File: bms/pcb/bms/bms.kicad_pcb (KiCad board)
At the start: 2 copper layers, 15 parts, among them U8 Pico

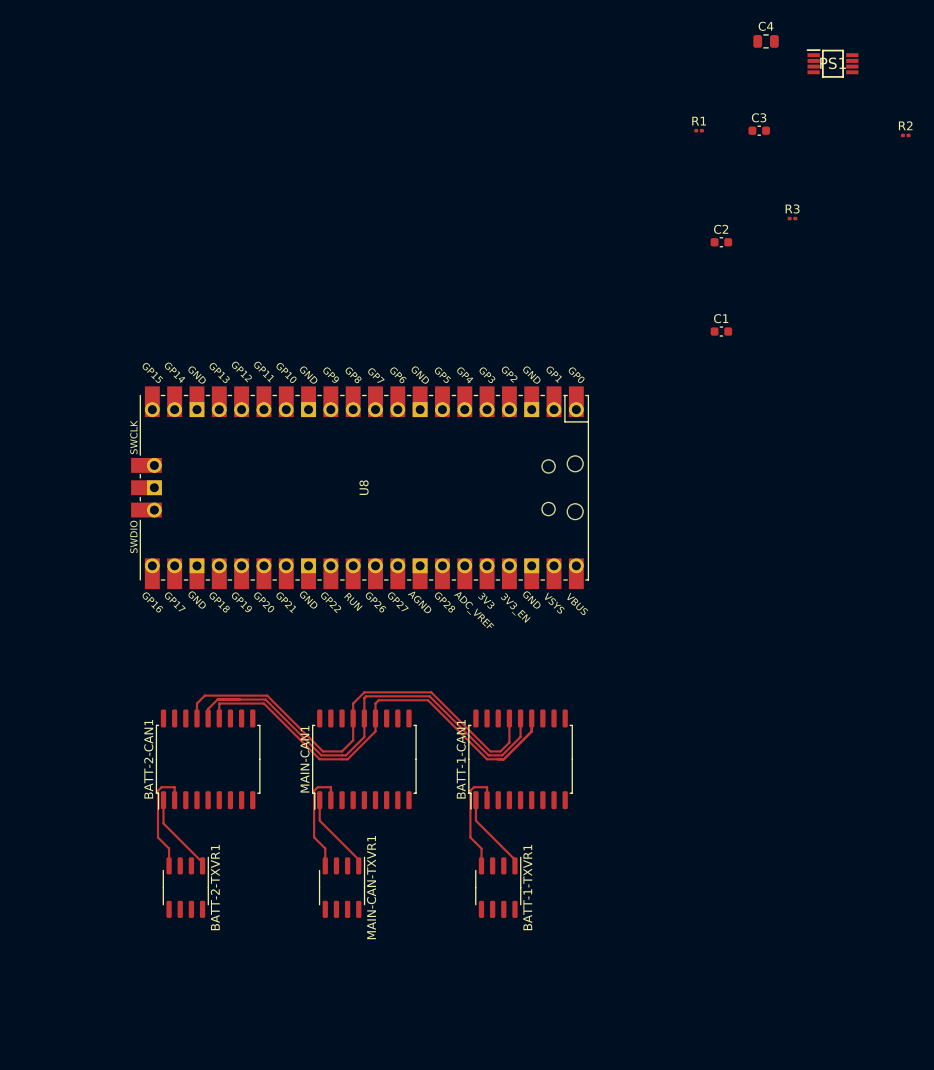
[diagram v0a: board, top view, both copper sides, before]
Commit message: v1.0 of BMS finalised. Sent of for fabrication
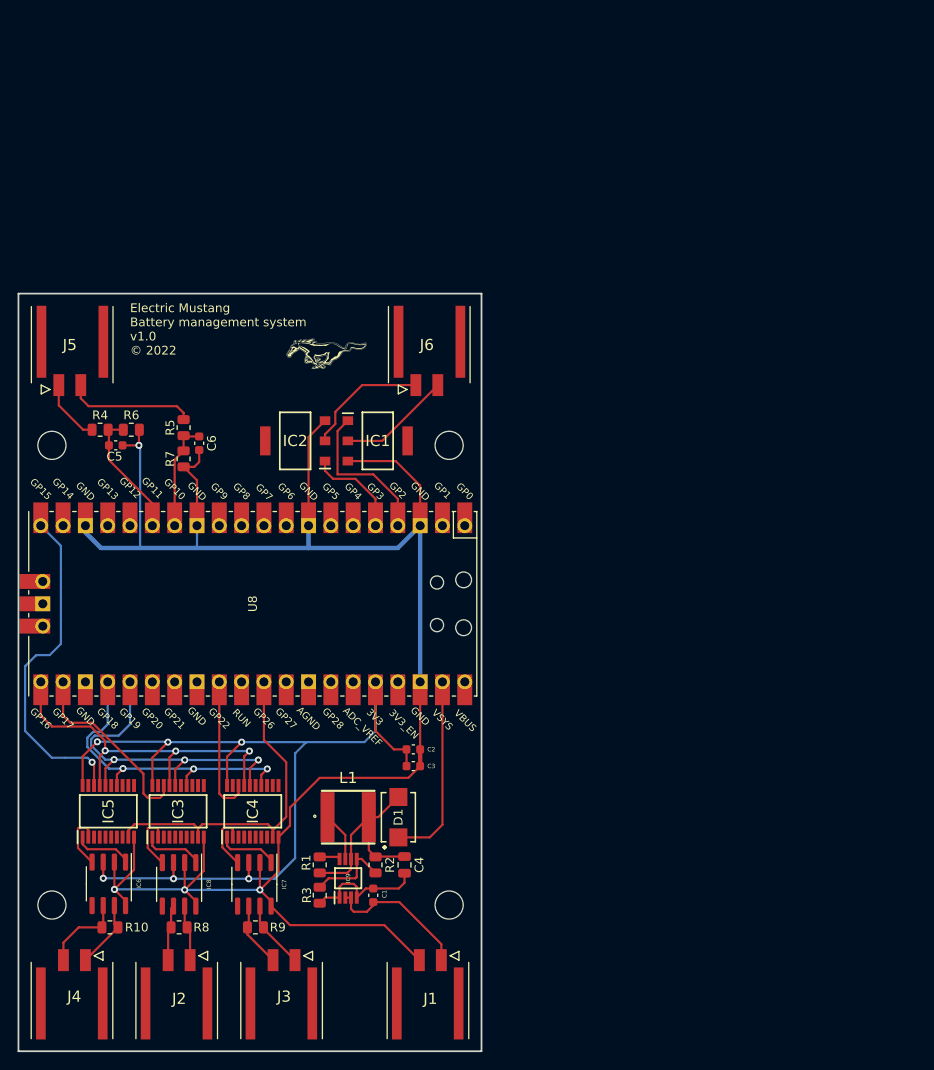
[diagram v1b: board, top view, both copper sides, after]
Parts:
- removed BATT-1-CAN1, BATT-2-CAN1, MAIN-CAN1: MCP2515-xSO, Package_SO:SOIC-18W_7.5x11.6mm_P1.27mm
- removed PS1: TPS62160DGKT, Module:SOP65P490X110-8N
- added C5: 1uF, Capacitor_SMD:C_0603_1608Metric, F.Cu at (80.9, 99.3)
- added C6: 1uF, Capacitor_SMD:C_0603_1608Metric, F.Cu at (90.4, 99.1)
- added D1: SS54B, Diode_SMD:DIOM5336X244N, F.Cu at (113.1, 141.6)
- added G***: LOGO, LOGO, F.Cu at (104.9, 88.9)
- added H1: MountingHole, MountingHole:MountingHole_3.2mm_M3, F.Cu at (73.7, 99.3)
- added H2: MountingHole, MountingHole:MountingHole_3.2mm_M3, F.Cu at (118.9, 99.3)
- added H3: MountingHole, MountingHole:MountingHole_3.2mm_M3, F.Cu at (118.9, 151.6)
- added H4: MountingHole, MountingHole:MountingHole_3.2mm_M3, F.Cu at (73.7, 151.6)
- added IC1: NCV8402ASTT1G, Symbol:SOT230P700X175-4N, F.Cu at (110.7, 98.8)
- added IC2: NCV8402ASTT1G, Symbol:SOT230P700X175-4N, F.Cu at (101.3, 98.8)
- added IC3: MCP2515-I_ST, Module:SOP65P640X120-20N, F.Cu at (88.0, 141.0)
- added IC4: MCP2515-I_ST, Module:SOP65P640X120-20N, F.Cu at (96.5, 141.0)
- added IC5: MCP2515-I_ST, Module:SOP65P640X120-20N, F.Cu at (80.1, 141.0)
- added IC9: TPS62160DGKR, Module:SOP65P490X110-8N, F.Cu at (107.4, 148.6)
- added J1: power, Connector:105430YY02, F.Cu at (116.7, 157.9)
- added J2: MAIN CAN, Connector:105430YY02, F.Cu at (88.1, 157.9)
- added J3: BATT1 CAN, Connector:105430YY02, F.Cu at (100.1, 157.9)
- added J4: BATT2 CAN, Connector:105430YY02, F.Cu at (76.2, 157.9)
- added J5: INPUTS, Connector:105430YY02, F.Cu at (75.7, 92.5)
- added J6: INPUTS, Connector:105430YY02, F.Cu at (116.3, 92.5)
- added L1: 2.2uH, Inductor_SMD:NR6028T220M, F.Cu at (107.4, 141.6)
- added R10: 120, Resistor_SMD:R_0805_2012Metric, F.Cu at (80.3, 154.2)
- added R4: 4k7, Resistor_SMD:R_0805_2012Metric, F.Cu at (79.1, 97.5)
- added R5: 4k7, Resistor_SMD:R_0805_2012Metric, F.Cu at (88.6, 97.3)
- added R6: 1k5, Resistor_SMD:R_0805_2012Metric, F.Cu at (82.7, 97.5)
- added R7: 1k5, Resistor_SMD:R_0805_2012Metric, F.Cu at (88.6, 100.9)
- added R8: 120, Resistor_SMD:R_0805_2012Metric, F.Cu at (88.1, 154.2)
- added R9: 120, Resistor_SMD:R_0805_2012Metric, F.Cu at (96.8, 154.2)
- R1, R2, R3: footprint Resistor_SMD:R_0201_0603Metric -> Resistor_SMD:R_0805_2012Metric
- moved R2 102.6 mm to (110.5, 147.1), turned to -90 degrees
- moved C4 102.4 mm to (113.8, 147.1), turned to -90 degrees
- moved R1 94.1 mm to (104.1, 147.1), turned to 90 degrees
- moved R3 94.0 mm to (104.1, 150.5), turned to -90 degrees
- moved C3 82.3 mm to (114.8, 135.8)
- moved C1 75.4 mm to (110.2, 150.5), turned to 90 degrees
- moved C2 67.5 mm to (114.8, 133.9)
- moved IC7 27.8 mm to (96.7, 149.3)
- moved IC8 18.5 mm to (88.1, 149.3)
- moved U8 18.3 mm to (96.5, 117.3)
- moved IC6 8.77 mm to (80.1, 149.2)
- renumbered BATT-2-TXVR1 to IC6, BATT-1-TXVR1 to IC7, MAIN-CAN-TXVR1 to IC8
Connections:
- U8 pad 1: unconnected-(U8-Pad1) -> UART_TX
- U8 pad 13: unconnected-(U8-Pad13) -> GND
- U8 pad 14: unconnected-(U8-Pad14) -> CHARGE_ENABLE_IN_SIGNAL
- U8 pad 15: unconnected-(U8-Pad15) -> IGNITION_ON_IN_SIGNAL
- U8 pad 18: unconnected-(U8-Pad18) -> GND
- U8 pad 2: unconnected-(U8-Pad2) -> UART_RX
- U8 pad 20: BATT_1_CS -> BATT_2_CS
- U8 pad 29: unconnected-(U8-Pad29) -> BATT_1_CS
- U8 pad 31: unconnected-(U8-Pad31) -> 8MHz
- U8 pad 38: unconnected-(U8-Pad38) -> GND
- U8 pad 4: unconnected-(U8-Pad4) -> BATT_1_CONTACTOR_SIGNAL
- U8 pad 42: GND -> unconnected-(U8-Pad42)
- U8 pad 5: unconnected-(U8-Pad5) -> BATT_2_CONTACTOR_SIGNAL
- U8 pad 7: SPI0_CS -> unconnected-(U8-Pad7)
- U8 pad 8: unconnected-(U8-Pad8) -> GND
- U8 pad 9: 8MHz -> unconnected-(U8-Pad9)
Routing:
- net GND: track 0.00 -> 219.8 mm, vias 0 -> 4
- net 3V: track 0.00 -> 108.7 mm, vias 0 -> 6
- net BATT_2_CS: track 0.00 -> 38.7 mm, vias 0 -> 1
- net 8MHz: track 0.00 -> 38.6 mm
- net 5V: track 0.00 -> 23.0 mm
- net Net-(D1-Pad1): track 0.00 -> 21.9 mm
- net MAIN_CAN_CS: track 0.00 -> 21.6 mm
- net SPI0_CLK: track 55.9 -> 37.0 mm, vias 0 -> 3
- net BATT_1_CONTACTOR_SIGNAL: track 0.00 -> 17.7 mm
- net 12V: track 0.00 -> 16.8 mm
- net BATT_1_CS: track 0.00 -> 16.2 mm
- net IGNITION_ON_IN_SIGNAL: track 0.00 -> 14.7 mm
- net CHARGE_ENABLE_IN: track 0.00 -> 14.7 mm
- net Net-(C1-Pad2): track 0.00 -> 14.4 mm
- net BATT_2_CONTACTOR_GND: track 0.00 -> 14.2 mm
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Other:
- board outline added: 52.7 x 86.2 mm
- board text added: "Electric Mustang Battery management system v1.0 © 2022"

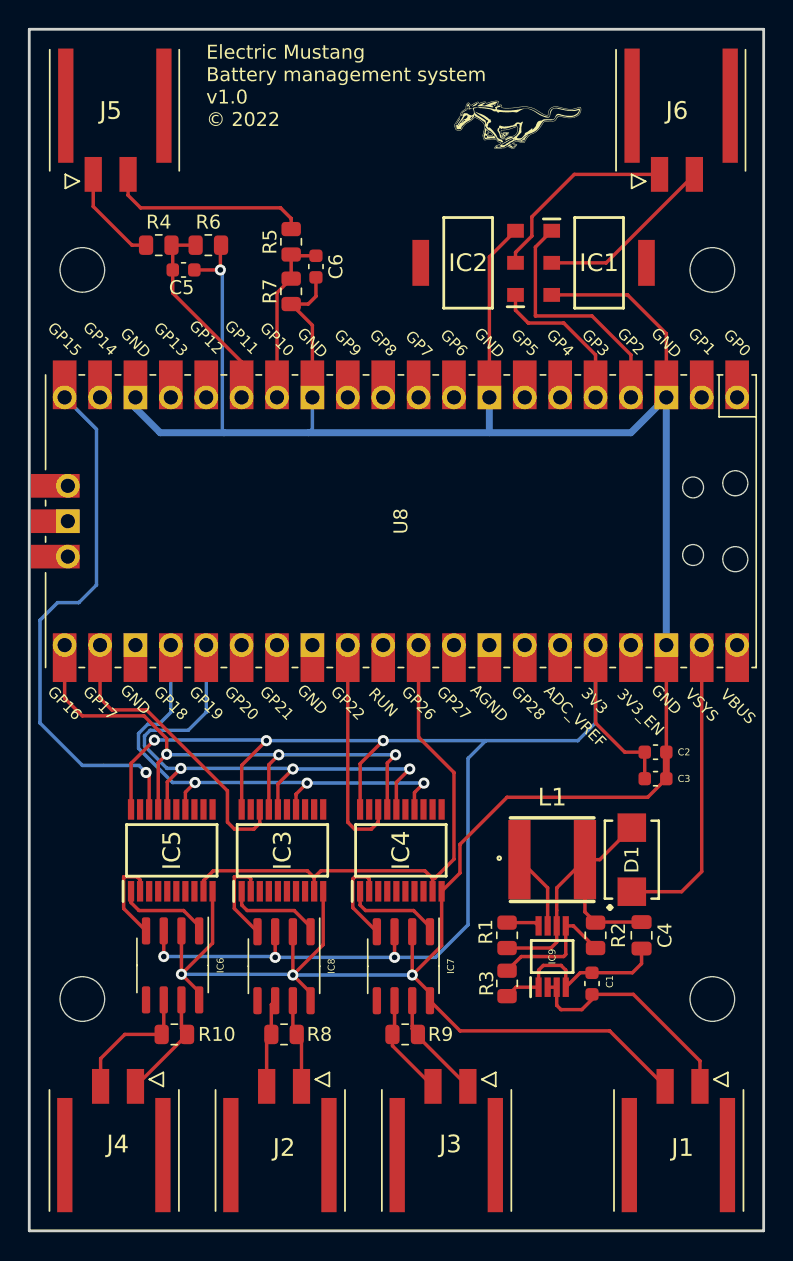
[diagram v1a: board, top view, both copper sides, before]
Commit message: BMS PCB fixes. Serial header for debugging. Heavier traces in certain places. Fix some pico pin connections.
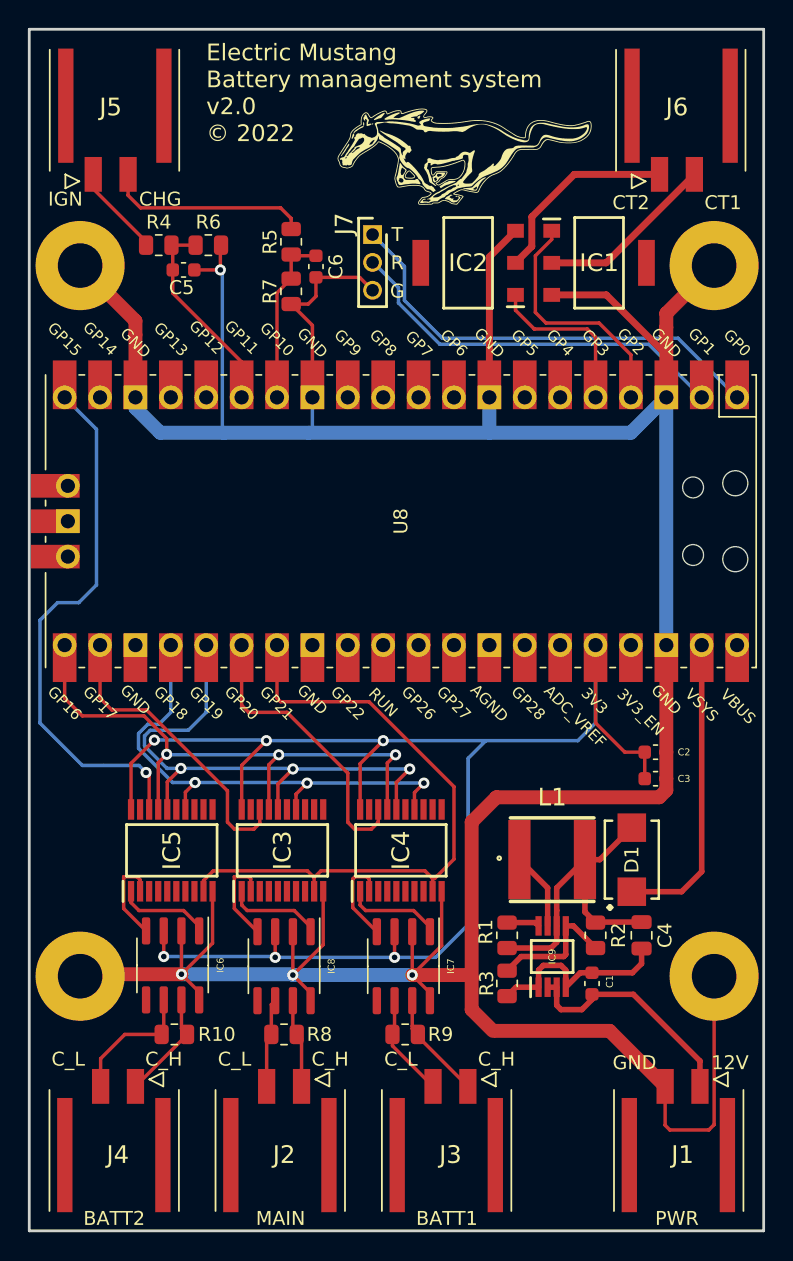
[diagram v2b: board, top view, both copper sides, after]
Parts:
- added J7: M22-2510346, Connector:HDRV3W50P0X200_1X3_600X200X525P, F.Cu at (94.5, 96.8)
- H1, H2, H3, H4: footprint MountingHole:MountingHole_3.2mm_M3 -> MountingHole:MountingHole_3.2mm_M3_Pad
- moved H3 45.4 mm to (73.5, 150.0)
- moved H4 45.4 mm to (119.0, 150.0)
- moved G*** 4.44 mm to (101.1, 91.2)
- moved H1 0.35 mm to (73.5, 99.0)
- moved H2 0.34 mm to (119.0, 99.0)
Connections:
- U8 pad 26: unconnected-(U8-Pad26) -> BATT_1_CS
- U8 pad 27: unconnected-(U8-Pad27) -> 8MHz
- U8 pad 29: BATT_1_CS -> unconnected-(U8-Pad29)
- U8 pad 31: 8MHz -> unconnected-(U8-Pad31)
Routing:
- net GND: track 219.8 -> 279.6 mm
- net UART_TX: track 0.00 -> 32.4 mm
- net UART_RX: track 0.00 -> 28.3 mm
- net 8MHz: track 38.6 -> 46.5 mm
- net BATT_1_CS: track 16.2 -> 21.0 mm
- net BATT_2_CONTACTOR_SIGNAL: track 11.2 -> 12.0 mm
- net IGNITION_ON_IN: track 7.25 -> 6.65 mm
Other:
- board text added: "12V"
- board text added: "BATT1"
- board text added: "BATT2"
- board text added: "CHG"
- board text added: "CT1"
- board text added: "CT2"
- board text added: "C_H"
- board text added: "C_L"
- board text added: "Electric Mustang Battery management system v2.0 © 2022"
- board text added: "G"
- board text added: "GND"
- board text added: "IGN"
- board text added: "MAIN"
- board text added: "PWR"
- board text added: "R"
- board text added: "T"
- board text removed: "Electric Mustang Battery management system v1.0 © 2022"
